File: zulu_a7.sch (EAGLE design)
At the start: 169 parts, among them J1 Pmod 2x6, Q1 12MHz 25ppm (FPGA + FT2232HQ), Q2 NMOS, Q3 MBT3904DW1T1, U1 XC7A35T-1CPG236C, U10 93LC46BT-I/SN, U2 FT2232HQ USB-UART/JTAG Bridge, U3 AS4C32M16SB-6TIN, U4 W25Q128JVSIQ, U8 LTC3569EUDC#TRPBF, X1 Molex 105017-0001 Micro-USB-B, X2 ZULU-CONN, X3 MICROSD_CONDM3AT-SF-PEJM5

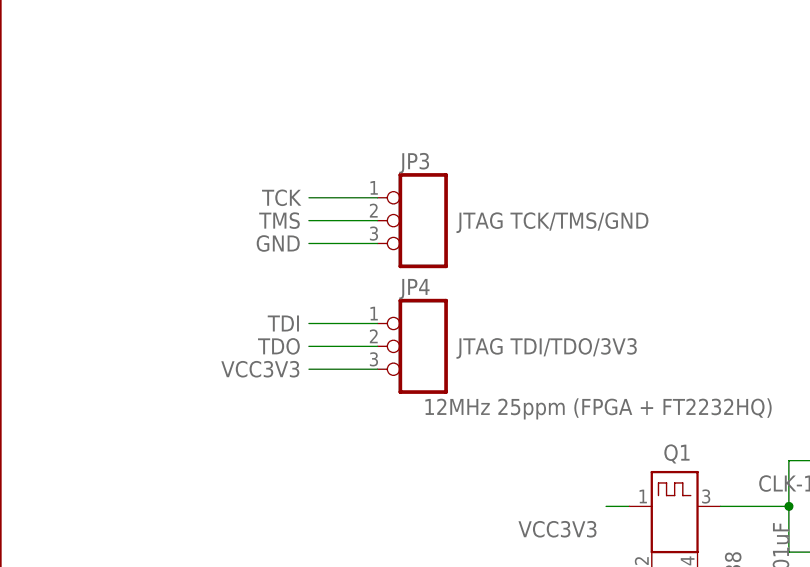
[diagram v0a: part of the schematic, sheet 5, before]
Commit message: Draw the JTAG as holes, because that is what it is
Two photographs settled it: the Pmod is a socket a module plugs into, the JTAG
is bare copper. Both were drawn as the same rectangle with numbered pins, so
the only thing telling them apart was the refdes prefix. That is the same
failure as the 2x3 -- a symbol promising a connector that is not there -- one
level up, in the drawing rather than the footprint.

So JP3 and JP4 stop looking like connectors:

  - the outline is dashed and 0.1524 wide, not solid 0.4064. Dashed is the
    ordinary way to say a body is not fitted, and it still groups the three.
  - each pin ends in an open circle: the plated hole itself.
  - function="dot" is gone. That bubble is a connector pin's; the hole is now
    drawn where the hole actually is.
  - symbol PINH1X3 -> TP1X3, deviceset PINHD-1X3 -> TESTPT-1X3. Leaving
    "PINHD" in the name would have kept the claim alive in the parts list
    after taking it out of the picture.

J1 keeps its solid box and its bubbles. It has earned them.

Both parts carry a NOTE saying no header is fitted and nothing is to be
ordered, which is the thing that actually stops a 1x3 strip appearing on a
BOM six months from now. The 0.09 mm to the Pmod shroud is recorded there as
what it is -- a clearance, not a collision. A strip fits; it just fits by
nothing, so the intent is written down instead of left to be inferred.

pinhead is now one symbol, one package, one deviceset, all used.
validate.py 0 findings; placement check 15 blocks, 0 parked.

Co-Authored-By: Claude Opus 5 <noreply@anthropic.com>
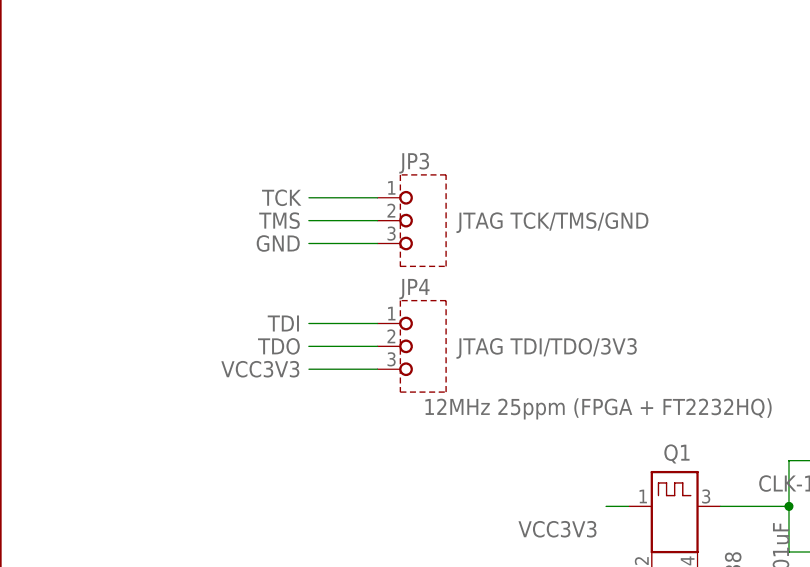
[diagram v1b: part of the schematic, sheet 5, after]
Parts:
- JP3, JP4: device pinhead:PINHD-1X3NOSILK -> pinhead:TESTPT-1X3NOSILK; NOTE (none) -> Bare plated holes -- NO HEADER FITTED, nothing to order. Th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
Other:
- moved on the sheet: JP3, JP4
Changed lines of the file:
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@@
 <attribute name="MANF" value="Microchip"/>
 </part>
-<part name="JP3" library="pinhead" deviceset="PINHD-1X3" device="NOSILK" value="JTAG TCK/TMS/GND"/>
-<part name="JP4" library="pinhead" deviceset="PINHD-1X3" device="NOSILK" value="JTAG TDI/TDO/3V3"/>
+<part name="JP3" library="pinhead" deviceset="TESTPT-1X3" device="NOSILK" value="JTAG TCK/TMS/GND">
+<attribute name="NOTE" value="Bare plated holes -- NO HEADER FITTED, nothing to order. Three of the six JTAG holes; JP4 carries the other three, 17.96 mm away on the far side of the Pmod. Each row has 3.05 mm of board to the Pmod but only 0.09 mm to a 1x3 strip's body, so these are for flying leads or a pogo jig. The FT2232 does JTAG over USB on channel B; this is the fallback."/>
+</part>
+<part name="JP4" library="pinhead" deviceset="TESTPT-1X3" device="NOSILK" value="JTAG TDI/TDO/3V3">
+<attribute name="NOTE" value="Bare plated holes -- NO HEADER FITTED, nothing to order. Three of the six JTAG holes; JP3 carries the other three, 17.96 mm away on the far side of the Pmod. Each row has 3.05 mm of board to the Pmod but only 0.09 mm to a 1x3 strip's body, so these are for flying leads or a pogo jig. The FT2232 does JTAG over USB on channel B; this is the fallback."/>
+</part>
 <part name="R4" library="ctambe" deviceset="RES8" device="741X" value="100">
 <attribute name="DIGIKEY#" value="741X163101JPCT-ND"/>

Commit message: The eight Pmod series resistors go 0402 -> 0201
R26-R33, the 200R in series with the Pmod's eight signal pins. New R0201
package in rcl and an R0201 device on R-US_SMALL; the parts keep their value,
their nets and their 1 % tolerance.

WHAT IT BOUGHT. All eight now sit in a 2x4 block at x 59.49 and 60.09, y 8.60
to 13.99, hard against J1 -- which is where a series resistor for a connector
pin belongs. R33 came off the hand-pin it needed two commits ago: at 0402 it
would not seat within 24 mm of J1 and had to be stranded at x 33; at 0201 the
anchored pass reaches it and it rejoined its seven siblings. Keepout per part
falls 2.95 x 0.97 to 1.75 x 0.37, about a quarter of the area.

THE POWER RATING IS THE THING TO KNOW. These resistors exist for one case: a
Pmod pin driven high into a short. That is 3.3 V across 200 R = 16.5 mA and
54.4 mW, sustained. An 0402 at 1/16 W has 62.5 mW and takes it at 87 %. An 0201
at 1/20 W has 50 mW and is at 109 % -- over rating, not under. It is a fault
case and not normal operation, and Cmod A7 evidently accepts the same, so this
follows that lead. But the margin that existed is gone, and a resistor that
cooks in the fault it was put there to survive is worth knowing about.

The land pattern is marked PROVISIONAL in the package, the way ESP-11 is. It is
0.30 x 0.30 pads on a 0.20 gap, a conventional 0201 land -- deliberately NOT
scaled from R0402 here, which carries a 0.50 mm toe that is generous for hand
work and would pull 0201 parts into tombstones. Check it against the maker's
recommendation and the assembler's 0201 capability before fabricating; 0201 is
not reworkable by hand.

Caught while doing it: the SPEC string "thick film +-1%, 1/16W, 0402" is shared
by 50 parts, so a blind replace relabelled 42 still-0402 resistors as 0201.
Every part's device and SPEC now agree, and the only R-parts without a SPEC are
the six that never had one.

157 placed, 8 real parts parked, unchanged. check_board and validate 0 findings.

Co-Authored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
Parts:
- R26, R27, R28, R29, R30, R31, R32, R33: device rcl:R-US_SMALLR0402 -> rcl:R-US_SMALLR0201; MANF# RC0402FR-07200RL -> RC0201FR-07200RL; SPEC thick film +-1%, 1/16W, 0402 -> thick film +-1%, 1/20W, 0201
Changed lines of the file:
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@@
 <part name="FRAME4" library="ctambe" deviceset="DOCFIELD" device=""/>
 <part name="FRAME3" library="ctambe" deviceset="DOCFIELD" device=""/>
-<part name="R26" library="rcl" deviceset="R-US_SMALL" device="R0402" value="200">
+<part name="R26" library="rcl" deviceset="R-US_SMALL" device="R0201" value="200">
 <attribute name="MANF" value="Yageo"/>
-<attribute name="MANF#" value="RC0402FR-07200RL"/>
-<attribute name="SPEC" value="thick film +-1%, 1/16W, 0402"/>
+<attribute name="MANF#" value="RC0201FR-07200RL"/>
+<attribute name="SPEC" value="thick film +-1%, 1/20W, 0201"/>
 </part>
-<part name="R27" library="rcl" deviceset="R-US_SMALL" device="R0402" value="200">
+<part name="R27" library="rcl" deviceset="R-US_SMALL" device="R0201" value="200">
 <attribute name="MANF" value="Yageo"/>
-<attribute name="MANF#" value="RC0402FR-07200RL"/>
-<attribute name="SPEC" value="thick film +-1%, 1/16W, 0402"/>
+<attribute name="MANF#" value="RC0201FR-07200RL"/>
+<attribute name="SPEC" value="thick film +-1%, 1/20W, 0201"/>
 </part>
-<part name="R28" library="rcl" deviceset="R-US_SMALL" device="R0402" value="200">
+<part name="R28" library="rcl" deviceset="R-US_SMALL" device="R0201" value="200">
 <attribute name="MANF" value="Yageo"/>
-<attribute name="MANF#" value="RC0402FR-07200RL"/>
-<attribute name="SPEC" value="thick film +-1%, 1/16W, 0402"/>
+<attribute name="MANF#" value="RC0201FR-07200RL"/>
+<attribute name="SPEC" value="thick film +-1%, 1/20W, 0201"/>
 </part>
-<part name="R29" library="rcl" deviceset="R-US_SMALL" device="R0402" value="200">
+<part name="R29" library="rcl" deviceset="R-US_SMALL" device="R0201" value="200">
 <attribute name="MANF" value="Yageo"/>
-<attribute name="MANF#" value="RC0402FR-07200RL"/>
-<attribute name="SPEC" value="thick film +-1%, 1/16W, 0402"/>
+<attribute name="MANF#" value="RC0201FR-07200RL"/>
+<attribute name="SPEC" value="thick film +-1%, 1/20W, 0201"/>
 </part>
-<part name="R30" library="rcl" deviceset="R-US_SMALL" device="R0402" value="200">
+<part name="R30" library="rcl" deviceset="R-US_SMALL" device="R0201" value="200">
 <attribute name="MANF" value="Yageo"/>
-<attribute name="MANF#" value="RC0402FR-07200RL"/>
-<attribute name="SPEC" value="thick film +-1%, 1/16W, 0402"/>
+<attribute name="MANF#" value="RC0201FR-07200RL"/>
+<attribute name="SPEC" value="thick film +-1%, 1/20W, 0201"/>
 </part>
-<part name="R31" library="rcl" deviceset="R-US_SMALL" device="R0402" value="200">
+<part name="R31" library="rcl" deviceset="R-US_SMALL" device="R0201" value="200">
 <attribute name="MANF" value="Yageo"/>
-<attribute name="MANF#" value="RC0402FR-07200RL"/>
-<attribute name="SPEC" value="thick film +-1%, 1/16W, 0402"/>
+<attribute name="MANF#" value="RC0201FR-07200RL"/>
+<attribute name="SPEC" value="thick film +-1%, 1/20W, 0201"/>
 </part>
-<part name="R32" library="rcl" deviceset="R-US_SMALL" device="R0402" value="200">
+<part name="R32" library="rcl" deviceset="R-US_SMALL" device="R0201" value="200">
 <attribute name="MANF" value="Yageo"/>
-<attribute name="MANF#" value="RC0402FR-07200RL"/>
-<attribute name="SPEC" value="thick film +-1%, 1/16W, 0402"/>
+<attribute name="MANF#" value="RC0201FR-07200RL"/>
+<attribute name="SPEC" value="thick film +-1%, 1/20W, 0201"/>
 </part>
-<part name="R33" library="rcl" deviceset="R-US_SMALL" device="R0402" value="200">
+<part name="R33" library="rcl" deviceset="R-US_SMALL" device="R0201" value="200">
 <attribute name="MANF" value="Yageo"/>
-<attribute name="MANF#" value="RC0402FR-07200RL"/>
-<attribute name="SPEC" value="thick film +-1%, 1/16W, 0402"/>
+<attribute name="MANF#" value="RC0201FR-07200RL"/>
+<attribute name="SPEC" value="thick film +-1%, 1/20W, 0201"/>
 </part>
 <part name="U$2" library="ctambe" deviceset="CC_CC" device=""/>

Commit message: The eight XADC resistors go 0603 -> 0201, and five parts come off the park
R10-R17, both XADC channels: the 2.32k/1k divider, the 140R into AIN_P and the
845R from AIN_N to ground. R-US_ gains an R0201 device; values, nets and 1 %
tolerance unchanged.

POWER IS NOT THE QUESTION HERE, unlike the Pmod eight. The only ones carrying
current are R10/R14 at the top of a 3.32k divider: 2.3 mW at a 3.3 V input,
5.3 mW at 5 V, against an 0201's 50 mW. Eleven per cent of rating at the worst
case, nine times the margin. R12/R13/R16/R17 sit on XADC inputs and carry
leakage. Nothing here cooks the way a shorted Pmod pin does.

Nor does size touch what this circuit depends on. R13 = 845R is matching
R12 + (R10||R11) = 838.8R so both XADC inputs see the same source impedance,
and that is a tolerance property. 1 % is 1 % at any size.

WHAT IT FREED. Parked real parts 8 -> 3. R15, R16 and R17 seated, and the space
released also let D3 and R5 in. The four that matter most are close: R12 5.6 mm
from the ball centre, R17 5.5, R16 6.2, R13 7.2 -- the network at the XADC pins
is tight to the package. R10/R11 and R14/R15 landed 20 to 24 mm out, which is
fine for a divider that only scales the input before it reaches that network.

WHAT IS LEFT: R1, R2 and R4, all three array packages, which no amount of chip
shrinking helps. Splitting them into 16 discrete 0402 is still the open option.

AND ONE THING TO LOOK AT. D3 is on the board now, at 51.3 mm from X2 pad 1. I
had left it parked on purpose because 55 mm from the pin a TVS protects is not
protection. Freeing space did not fix that -- it just let the anchored pass seat
it, at the far end, where it clamps no better than it did unplaced. It now looks
placed. It is not placed usefully, and dropping JP3/JP4 is still what would give
it the corner it wants.

161 placed. check_board and validate 0 findings.

Co-Authored-By: Claude Opus 5 <noreply@anthropic.com>
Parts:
- R10, R14: device rcl:R-US_R0603 -> rcl:R-US_R0201; MANF# RC0603FR-072K32L -> RC0201FR-072K32L; SPEC thick film +-1%, 1/16W, 0603 -> thick film +-1%, 1/20W, 0201
- R11, R15: device rcl:R-US_R0603 -> rcl:R-US_R0201; MANF# RC0603FR-071KL -> RC0201FR-071KL; SPEC thick film +-1%, 1/16W, 0603 -> thick film +-1%, 1/20W, 0201
- R12, R16: device rcl:R-US_R0603 -> rcl:R-US_R0201; MANF# RC0603FR-07140RL -> RC0201FR-07140RL; SPEC thick film +-1%, 1/16W, 0603 -> thick film +-1%, 1/20W, 0201
- R13, R17: device rcl:R-US_R0603 -> rcl:R-US_R0201; MANF# RC0603FR-07845RL -> RC0201FR-07845RL; SPEC thick film +-1%, 1/16W, 0603 -> thick film +-1%, 1/20W, 0201
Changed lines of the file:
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@@
 <attribute name="MANF" value="AMD/Xilinx"/>
 </part>
-<part name="R10" library="rcl" deviceset="R-US_" device="R0603" value="2.32K">
+<part name="R10" library="rcl" deviceset="R-US_" device="R0201" value="2.32K">
 <attribute name="MANF" value="Yageo"/>
-<attribute name="MANF#" value="RC0603FR-072K32L"/>
-<attribute name="SPEC" value="thick film +-1%, 1/16W, 0603"/>
+<attribute name="MANF#" value="RC0201FR-072K32L"/>
+<attribute name="SPEC" value="thick film +-1%, 1/20W, 0201"/>
 </part>
-<part name="R11" library="rcl" deviceset="R-US_" device="R0603" value="1K">
+<part name="R11" library="rcl" deviceset="R-US_" device="R0201" value="1K">
 <attribute name="MANF" value="Yageo"/>
-<attribute name="MANF#" value="RC0603FR-071KL"/>
-<attribute name="SPEC" value="thick film +-1%, 1/16W, 0603"/>
+<attribute name="MANF#" value="RC0201FR-071KL"/>
+<attribute name="SPEC" value="thick film +-1%, 1/20W, 0201"/>
 </part>
-<part name="R12" library="rcl" deviceset="R-US_" device="R0603" value="140">
+<part name="R12" library="rcl" deviceset="R-US_" device="R0201" value="140">
 <attribute name="MANF" value="Yageo"/>
-<attribute name="MANF#" value="RC0603FR-07140RL"/>
-<attribute name="SPEC" value="thick film +-1%, 1/16W, 0603"/>
+<attribute name="MANF#" value="RC0201FR-07140RL"/>
+<attribute name="SPEC" value="thick film +-1%, 1/20W, 0201"/>
 </part>
-<part name="R13" library="rcl" deviceset="R-US_" device="R0603" value="845">
+<part name="R13" library="rcl" deviceset="R-US_" device="R0201" value="845">
 <attribute name="MANF" value="Yageo"/>
-<attribute name="MANF#" value="RC0603FR-07845RL"/>
-<attribute name="SPEC" value="thick film +-1%, 1/16W, 0603"/>
+<attribute name="MANF#" value="RC0201FR-07845RL"/>
+<attribute name="SPEC" value="thick film +-1%, 1/20W, 0201"/>
 </part>
-<part name="R14" library="rcl" deviceset="R-US_" device="R0603" value="2.32K">
+<part name="R14" library="rcl" deviceset="R-US_" device="R0201" value="2.32K">
 <attribute name="MANF" value="Yageo"/>
-<attribute name="MANF#" value="RC0603FR-072K32L"/>
-<attribute name="SPEC" value="thick film +-1%, 1/16W, 0603"/>
+<attribute name="MANF#" value="RC0201FR-072K32L"/>
+<attribute name="SPEC" value="thick film +-1%, 1/20W, 0201"/>
 </part>
-<part name="R15" library="rcl" deviceset="R-US_" device="R0603" value="1K">
+<part name="R15" library="rcl" deviceset="R-US_" device="R0201" value="1K">
 <attribute name="MANF" value="Yageo"/>
-<attribute name="MANF#" value="RC0603FR-071KL"/>
-<attribute name="SPEC" value="thick film +-1%, 1/16W, 0603"/>
+<attribute name="MANF#" value="RC0201FR-071KL"/>
+<attribute name="SPEC" value="thick film +-1%, 1/20W, 0201"/>
 </part>
-<part name="R16" library="rcl" deviceset="R-US_" device="R0603" value="140">
+<part name="R16" library="rcl" deviceset="R-US_" device="R0201" value="140">
 <attribute name="MANF" value="Yageo"/>
-<attribute name="MANF#" value="RC0603FR-07140RL"/>
-<attribute name="SPEC" value="thick film +-1%, 1/16W, 0603"/>
+<attribute name="MANF#" value="RC0201FR-07140RL"/>
+<attribute name="SPEC" value="thick film +-1%, 1/20W, 0201"/>
 </part>
-<part name="R17" library="rcl" deviceset="R-US_" device="R0603" value="845">
+<part name="R17" library="rcl" deviceset="R-US_" device="R0201" value="845">
 <attribute name="MANF" value="Yageo"/>
-<attribute name="MANF#" value="RC0603FR-07845RL"/>
-<attribute name="SPEC" value="thick film +-1%, 1/16W, 0603"/>
+<attribute name="MANF#" value="RC0201FR-07845RL"/>
+<attribute name="SPEC" value="thick film +-1%, 1/20W, 0201"/>
 </part>
 <part name="C3" library="rcl" deviceset="C-GENERIC" device="C0402" value="0.1uF">

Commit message: Split R1, R2 and R4 into eleven discretes; one part left parked
R1 and R2 to 0201, R4 to 0402, as agreed. The arrays fitted NOWHERE -- a
742C083 needs 3.55 x 3.35 and the largest free square on this board was 2.9 x
2.9 front, 2.1 x 2.1 back -- so they were not short of a good spot, they were
short of any spot.

FIVE OF THE SIXTEEN ELEMENTS WERE NEVER CONNECTED. R1 used 2 of 4, R2 used 3 of
4, R4 used 6 of 8. Three arrays were holding 25.4 mm2 of a board with no room
in order to deliver eleven resistors. That is the real find; the size change is
secondary.

THE SYMBOL DID NOT CHANGE, WHICH IS WHY NO WIRE MOVED. R1NV0, the symbol the
arrays drew their elements with, has its pins 10.16 mm apart; R-US_SMALL has
them 5.08. Swapping to the discrete symbol would have pulled both pins 2.54 mm
inward on all eleven and stranded every net that touched them. So R1NV0 is
copied into rcl and a new deviceset R-WIDE hangs the R0201 and R0402 packages
off it. Each instance keeps its x, y and rotation; only the part behind it
changed. Net membership is identical, checked pin by pin against the old gates.

  R1.A -> R1   R1.B -> R3                       4.7k pull-ups/downs, 0201
  R2.A -> R2   R2.B -> R6   R2.D -> R7          4.7k flash pull-ups, 0201
  R4.A -> R4   R4.B -> R8   R4.C -> R9
  R4.F -> R36  R4.G -> R37  R4.H -> R38         100R JTAG series, 0402

R4 stayed 0402 on purpose. Contention through 100R is 109 mW from an ideal
source and 30-50 mW once the drivers' own impedance is counted; that is 60-100 %
of an 0201 and 48-80 % of an 0402. The 741X163 it replaces is a 1/16 W part, so
0402 keeps the rating the design had.

RES8 went with it, and 741X163, 742C163, 743C163, 744C163 and SOCKED-16 with
that -- 335 lines. RES4 stays: R34 is still a 4-pack.

Parked real parts 3 -> 1. 171 placed. Only R90 is left, a 10k pull-up on TDI,
and a pull-up is the least position-critical thing on the board.

Placement is uneven and worth knowing: R9 landed 4.3 mm from U1 and R38 7.3,
but the 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
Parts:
- added R3, R6, R7: 4.7K, rcl:R-WIDER0201
- added R36, R37, R38, R8, R9: 100, rcl:R-WIDER0402
- R1, R2: device ctambe:RES4742 -> rcl:R-WIDER0201; DIGIKEY# 742C083472JPCT-ND -> (none); MANF (none) -> Yageo; MANF# 742C083472JPTR -> RC0201FR-074K7L; MOUSER# 774-742C083472JP -> (none); SPEC (none) -> thick film +-1%, 1/20W, 0201
- R4: device ctambe:RES8741X -> rcl:R-WIDER0402; DIGIKEY# 741X163101JPCT-ND -> (none); MANF CTS -> Yageo; MANF# 741X163101JP -> RC0402FR-07100RL; MOUSER# 774-741X163101JP -> (none); SPEC (none) -> thick film +-1%, 1/16W, 0402
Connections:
- net DONE: now also R38.1; no longer R4H.1
- net FLASH-CS#: now also R7.1; no longer R2D.1
- net FLASH-D02: now also R2.1; no longer R2A.1
- net FLASH-D03: now also R6.1; no longer R2B.1
- net FPGA-DONE: now also R38.2; no longer R4H.2
- net FPGA-INIT#: now also R1.1; no longer R1A.1
- net FPGA-TCK: now also R36.2; no longer R4F.2
- net FPGA-TDI: now also R8.2; no longer R4B.2
- net FPGA-TDO: now also R37.2; no longer R4G.2
- net FPGA-TMS: now also R4.2; no longer R4A.2
- net GND: now also R3.2; no longer R1B.2
- net PROG#: now also R9.1; no longer R4C.1
- net RST#: now also R3.1, R9.2; no longer R1B.1, R4C.2
- net TCK: now also R36.1; no longer R4F.1
- net TDI: now also R8.1; no longer R4B.1
- net TDO: now also R37.1; no longer R4G.1
- net TMS: now also R4.1; no longer R4A.1
- net VCC3V3: now also R1.2, R2.2, R6.2, R7.2; no longer R1A.2, R2A.2, R2B.2, R2D.2
